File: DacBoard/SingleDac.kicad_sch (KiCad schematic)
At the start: 1 part, among them U5 AD5725

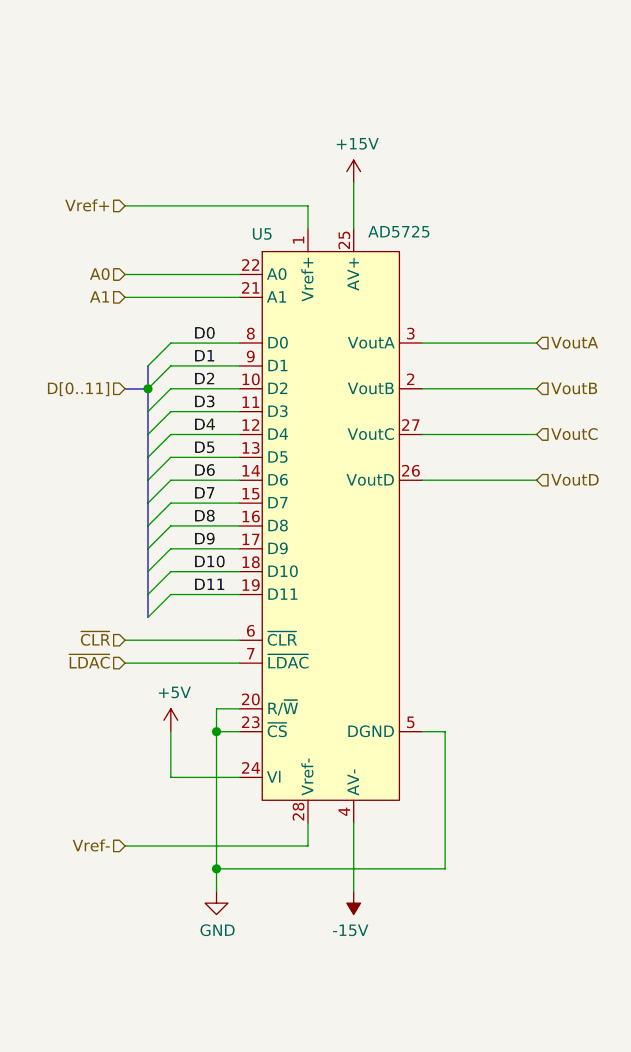
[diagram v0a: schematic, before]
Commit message: Changed data bus to single wires
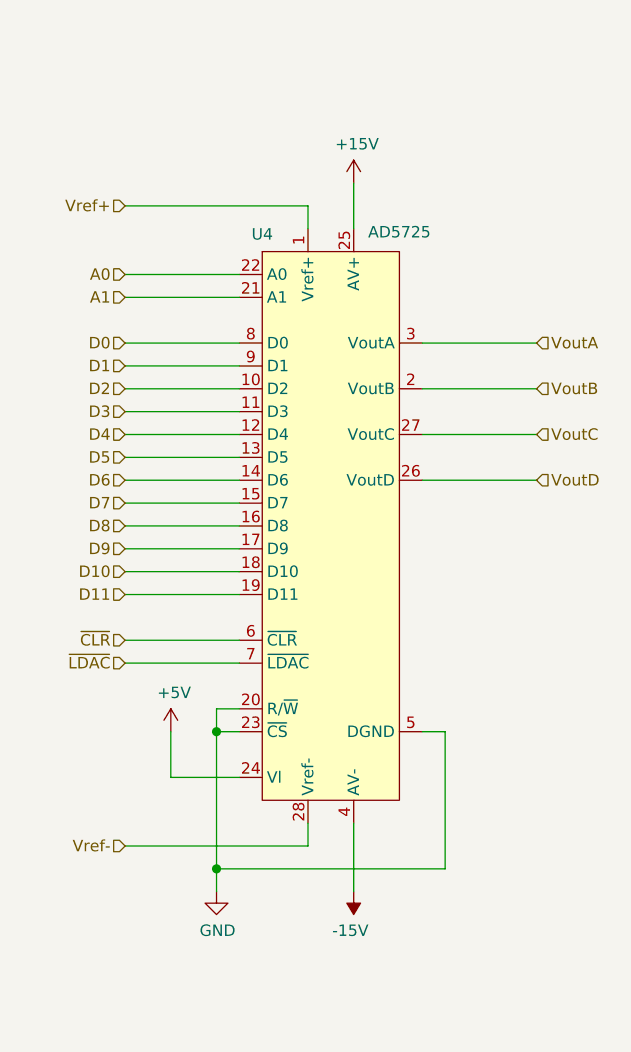
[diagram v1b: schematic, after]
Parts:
- renumbered U5 to U4

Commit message: Added bypass caps and moved PWR_FLAGs around
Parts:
- added C8, C9: 100n, symbol Device:C_Small
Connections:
- net +15V: now also C8.1, C8.2
- net -15V: now also C9.1, C9.2
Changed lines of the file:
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@@
   (paper "A4")
   (junction (at 167.64 104.14) (diameter 1.016) (color 0 0 0 0))
-  (junction (at 167.64 119.38) (diameter 1.016) (color 0 0 0 0))
+  (junction (at 182.88 33.02) (diameter 1.016) (color 0 0 0 0))
+  (junction (at 182.88 43.18) (diameter 1.016) (color 0 0 0 0))
+  (junction (at 182.88 121.92) (diameter 1.016) (color 0 0 0 0))
+  (junction (at 182.88 132.08) (diameter 1.016) (color 0 0 0 0))
   (wire (pts (xy 157.48 45.72) (xy 177.8 45.72))
     (stroke (width 0) (type solid) (color 0 0 0 0))
@@
     (stroke (width 0) (type solid) (color 0 0 0 0))
   )
-  (wire (pts (xy 167.64 104.14) (xy 167.64 119.38))
+  (wire (pts (xy 167.64 104.14) (xy 167.64 111.76))
     (stroke (width 0) (type solid) (color 0 0 0 0))
   )
@@
     (stroke (width 0) (type solid) (color 0 0 0 0))
   )
-  (wire (pts (xy 167.64 119.38) (xy 167.64 121.92))
-    (stroke (width 0) (type solid) (color 0 0 0 0))
-  )
-  (wire (pts (xy 167.64 119.38) (xy 193.04 119.38))
-    (stroke (width 0) (type solid) (color 0 0 0 0))
-  )
   (wire (pts (xy 170.18 101.6) (xy 167.64 101.6))
     (stroke (width 0) (type solid) (color 0 0 0 0))
@@
     (stroke (width 0) (type solid) (color 0 0 0 0))
   )
-  (wire (pts (xy 177.8 114.3) (xy 177.8 116.84))
-    (stroke (width 0) (type solid) (color 0 0 0 0))
-  )
-  (wire (pts (xy 177.8 116.84) (xy 157.48 116.84))
+  (wire (pts (xy 177.8 114.3) (xy 177.8 119.38))
+    (stroke (width 0) (type solid) (color 0 0 0 0))
+  )
+  (wire (pts (xy 177.8 119.38) (xy 157.48 119.38))
+    (stroke (width 0) (type solid) (color 0 0 0 0))
+  )
+  (wire (pts (xy 182.88 33.02) (xy 182.88 43.18))
+    (stroke (width 0) (type solid) (color 0 0 0 0))
+  )
+  (wire (pts (xy 182.88 33.02) (xy 187.96 33.02))
     (stroke (width 0) (type solid) (color 0 0 0 0))
   )
@@
     (stroke (width 0) (type solid) (color 0 0 0 0))
   )
+  (wire (pts (xy 182.88 43.18) (xy 187.96 43.18))
+    (stroke (width 0) (type solid) (color 0 0 0 0))
+  )
   (wire (pts (xy 182.88 114.3) (xy 182.88 121.92))
     (stroke (width 0) (type solid) (color 0 0 0 0))
   )
+  (wire (pts (xy 182.88 121.92) (xy 187.96 121.92))
+    (stroke (width 0) (type solid) (color 0 0 0 0))
+  )
+  (wire (pts (xy 182.88 132.08) (xy 182.88 121.92))
+    (stroke (width 0) (type solid) (color 0 0 0 0))
+  )
+  (wire (pts (xy 182.88 132.08) (xy 187.96 132.08))
+    (stroke (width 0) (type solid) (color 0 0 0 0))
+  )
+  (wire (pts (xy 187.96 33.02) (xy 187.96 35.56))
+    (stroke (width 0) (type solid) (color 0 0 0 0))
+  )
+  (wire (pts (xy 187.96 43.18) (xy 187.96 40.64))
+    (stroke (width 0) (type solid) (color 0 0 0 0))
+  )
+  (wire (pts (xy 187.96 121.92) (xy 187.96 124.46))
+    (stroke (width 0) (type solid) (color 0 0 0 0))
+  )
+  (wire (pts (xy 187.96 132.08) (xy 187.96 129.54))
+    (stroke (width 0) (type solid) (color 0 0 0 0))
+  )
   (wire (pts (xy 190.5 60.96) (xy 203.2 60.96))
     (stroke (width 0) (type solid) (color 0 0 0 0))
@@
     (stroke (width 0) (type solid) (color 0 0 0 0))
   )
-  (wire (pts (xy 193.04 104.14) (xy 193.04 119.38))
+  (wire (pts (xy 193.04 104.14) (xy 193.04 109.22))
     (stroke (width 0) (type solid) (color 0 0 0 0))
   )
@@
     (effects (font (size 1.27 1.27)) (justify right))
   )
-  (hierarchical_label "Vref-" (shape input) (at 157.48 116.84 180)
-    (effects (font (size 1.27 1.27)) (justify right))
-  )
-  (hierarchical_label "VoutA" (shape input) (at 203.2 60.96 0)
+  (hierarchical_label "Vref-" (shape input) (at 157.48 119.38 180)
+    (effects (font (size 1.27 1.27)) (justify right))
+  )
+  (hierarchical_label "VoutA" (shape output) (at 203.2 60.96 0)
     (effects (font (size 1.27 1.27)) (justify left))
   )
-  (hierarchical_label "VoutB" (shape input) (at 203.2 66.04 0)
+  (hierarchical_label "VoutB" (shape output) (at 203.2 66.04 0)
     (effects (font (size 1.27 1.27)) (justify left))
   )
-  (hierarchical_label "VoutC" (shape input) (at 203.2 71.12 0)
+  (hierarchical_label "VoutC" (shape output) (at 203.2 71.12 0)
     (effects (font (size 1.27 1.27)) (justify left))
   )
-  (hierarchical_label "VoutD" (shape input) (at 203.2 76.2 0)
+  (hierarchical_label "VoutD" (shape output) (at 203.2 76.2 0)
     (effects (font (size 1.27 1.27)) (justify left))
   )
@@
     (pin "1")
   )
-  (symbol (lib_id "power:+15V") (at 182.88 43.18 0)
-    (in_bom yes) (on_board yes)
-    (property "Reference" "#PWR05" (id 0) (at 182.88 46.99 0)
-      (effects (font (size 1.27 1.27)) hide)
-    )
-    (property "Value" "+15V" (id 1) (at 183.2483 38.8556 0))
-    (property "Footprint" "" (id 2) (at 182.88 43.18 0)
-      (effects (font (size 1.27 1.27)) hide)
-    )
-    (property "Datasheet" "" (id 3) (at 182.88 43.18 0)
-      (effects (font (size 1.27 1.27)) hide)
-    )
-    (pin "1")
-  )
-  (symbol (lib_id "power:-15V") (at 182.88 121.92 180)
-    (in_bom yes) (on_board yes)
-    (property "Reference" "#PWR06" (id 0) (at 182.88 124.46 0)
-      (effects (font (size 1.27 1.27)) hide)
-    )
-    (property "Value" "-15V" (id 1) (at 182.5117 126.2444 0))
-    (property "Footprint" "" (id 2) (at 182.88 121.92 0)
-      (effects (font (size 1.27 1.27)) hide)
-    )
-    (property "Datasheet" "" (id 3) (at 182.88 121.92 0)
-      (effects (font (size 1.27 1.27)) hide)
-    )
-    (pin "1")
-  )
-  (symbol (lib_id "power:GND") (at 167.64 121.92 0)
-    (in_bom yes) (on_board yes)
-    (property "Reference" "#PWR04" (id 0) (at 167.64 128.27 0)
-      (effects (font (size 1.27 1.27)) hide)
-    )
-    (property "Value" "GND" (id 1) (at 167.7543 126.2444 0))
-    (property "Footprint" "" (id 2) (at 167.64 121.92 0)
-      (effects (font (size 1.27 1.27)) hide)
-    )
-    (property "Datasheet" "" (id 3) (at 167.64 121.92 0)
-      (effects (font (size 1.27 1.27)) hide)
-    )
-    (pin "1")
+  (symbol (lib_id "power:+15V") (at 182.88 33.02 0)
+    (in_bom yes) (on_board yes)
+    (property "Reference" "#PWR05" (id 0) (at 182.88 36.83 0)
+      (effects (font (size 1.27 1.27)) hide)
+    )
+    (property "Value" "+15V" (id 1) (at 183.2483 28.6956 0))
+    (property "Footprint" "" (id 2) (at 182.88 33.02 0)
+      (effects (font (size 1.27 1.27)) hide)
+    )
+    (property "Datasheet" "" (id 3) (at 182.88 33.02 0)
+      (effects (font (size 1.27 1.27)) hide)
+    )
+    (pin "1")
+  )
+  (symbol (lib_id "power:-15V") (at 182.88 132.08 180)
+    (in_bom yes) (on_board yes)
+    (property "Reference" "#PWR06" (id 0) (at 182.88 134.62 0)
+      (effects (font (size 1.27 1.27)) hide)
+    )
+    (property "Value" "-15V" (id 1) (at 182.5117 136.4044 0))
+    (property "Footprint" "" (id 2) (at 182.88 132.08 0)
+      (effects (font (size 1.27 1.27)) hide)
+    )
+    (property "Datasheet" "" (id 3) (at 182.88 132.08 0)
+      (effects (font (size 1.27 1.27)) hide)
+    )
+    (pin "1")
+  )
+  (symbol (lib_id "power:GND") (at 167.64 111.76 0)
+    (in_bom yes) (on_board yes)
+    (property "Reference" "#PWR04" (id 0) (at 167.64 118.11 0)
+      (effects (font (size 1.27 1.27)) hide)
+    )
+    (property "Value" "GND" (id 1) (at 167.7543 116.0844 0))
+    (property "Footprint" "" (id 2) (at 167.64 111.76 0)
+      (effects (font (size 1.27 1.27)) hide)
+    )
+    (property "Datasheet" "" (id 3) (at 167.64 111.76 0)
+      (effects (font (size 1.27 1.27)) hide)
+    )
+    (pin "1")
+  )
+  (symbol (lib_id "power:GND") (at 193.04 109.22 0)
+    (in_bom yes) (on_board yes)
+    (property "Reference" "#PWR07" (id 0) (at 193.04 115.57 0)
+      (effects (font (size 1.27 1.27)) hide)
+    )
+    (property "Value" "GND" (id 1) (at 193.1543 113.5444 0))
+    (property "Footprint" "" (id 2) (at 193.04 109.22 0)
+      (effects (font (size 1.27 1.27)) hide)
+    )
+    (property "Datasheet" "" (id 3) (at 193.04 109.22 0)
+      (effects (font (size 1.27 1.27)) hide)
+    )
+    (pin "1")
+  )
+  (symbol (lib_id "Device:C_Small") (at 187.96 38.1 0)
+    (in_bom yes) (on_board yes)
+    (property "Reference" "C8" (id 0) (at 190.2842 36.9506 0)
+      (effects (font (size 1.27 1.27)) (justify left))
+    )
+    (property "Value" "100n" (id 1) (at 190.2968 39.243 0)
+      (effects (font (size 1.27 1.27)) (justify left))
+    )
+    (property "Footprint" "" (id 2) (at 187.96 38.1 0)
+      (effects (font (size 1.27 1.27)) hide)
+    )
+    (property "Datasheet" "~" (id 3) (at 187.96 38.1 0)
+      (effects (font (size 1.27 1.27)) hide)
+    )
+    (pin "1")
+    (pin "2")
+  )
+  (symbol (lib_id "Device:C_Small") (at 187.96 127 0)
+    (in_bom yes) (on_board yes)
+    (property "Reference" "C9" (id 0) (at 190.2842 125.8506 0)
+      (effects (font (size 1.27 1.27)) (justify left))
+    )
+    (property "Value" "100n" (id 1) (at 190.2968 128.143 0)
+      (effects (font (size 1.27 1.27)) (justify left))
+    )
+    (property "Footprint" "" (id 2) (at 187.96 127 0)
+      (effects (font (size 1.27 1.27)) hide)
+    )
+    (property "Datasheet" "~" (id 3) (at 187.96 127 0)
+      (effects (font (size 1.27 1.27)) hide)
+    )
+    (pin "1")
+    (pin "2")
   )
   (symbol (lib_id "Unichip:AD5725") (at 180.34 50.8 0)

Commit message: Fixed description of enable signal generators
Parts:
- renumbered C8 to C10, C9 to C11, U4 to U5
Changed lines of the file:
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@@
   (symbol (lib_id "power:+5V") (at 162.56 104.14 0)
     (in_bom yes) (on_board yes)
-    (property "Reference" "#PWR03" (id 0) (at 162.56 107.95 0)
+    (property "Reference" "#PWR0129" (id 0) (at 162.56 107.95 0)
       (effects (font (size 1.27 1.27)) hide)
     )
@@
   (symbol (lib_id "power:+15V") (at 182.88 33.02 0)
     (in_bom yes) (on_board yes)
-    (property "Reference" "#PWR05" (id 0) (at 182.88 36.83 0)
+    (property "Reference" "#PWR0128" (id 0) (at 182.88 36.83 0)
       (effects (font (size 1.27 1.27)) hide)
     )
@@
   (symbol (lib_id "power:-15V") (at 182.88 132.08 180)
     (in_bom yes) (on_board yes)
-    (property "Reference" "#PWR06" (id 0) (at 182.88 134.62 0)
+    (property "Reference" "#PWR0131" (id 0) (at 182.88 134.62 0)
       (effects (font (size 1.27 1.27)) hide)
     )
@@
   (symbol (lib_id "power:GND") (at 167.64 111.76 0)
     (in_bom yes) (on_board yes)
-    (property "Reference" "#PWR04" (id 0) (at 167.64 118.11 0)
+    (property "Reference" "#PWR0130" (id 0) (at 167.64 118.11 0)
       (effects (font (size 1.27 1.27)) hide)
     )
@@
   (symbol (lib_id "power:GND") (at 193.04 109.22 0)
     (in_bom yes) (on_board yes)
-    (property "Reference" "#PWR07" (id 0) (at 193.04 115.57 0)
+    (property "Reference" "#PWR08" (id 0) (at 193.04 115.57 0)
       (effects (font (size 1.27 1.27)) hide)
     )
@@
   (symbol (lib_id "Device:C_Small") (at 187.96 38.1 0)
     (in_bom yes) (on_board yes)
-    (property "Reference" "C8" (id 0) (at 190.2842 36.9506 0)
+    (property "Reference" "C10" (id 0) (at 190.2842 36.9506 0)
       (effects (font (size 1.27 1.27)) (justify left))
     )
@@
   (symbol (lib_id "Device:C_Small") (at 187.96 127 0)
     (in_bom yes) (on_board yes)
-    (property "Reference" "C9" (id 0) (at 190.2842 125.8506 0)
+    (property "Reference" "C11" (id 0) (at 190.2842 125.8506 0)
       (effects (font (size 1.27 1.27)) (justify left))
     )
@@
   (symbol (lib_id "Unichip:AD5725") (at 180.34 50.8 0)
     (in_bom yes) (on_board yes)
-    (property "Reference" "U4" (id 0) (at 172.72 48.8758 0))
+    (property "Reference" "U5" (id 0) (at 172.72 48.8758 0))
     (property "Value" "AD5725" (id 1) (at 187.96 48.6345 0))
     (property "Footprint" "Package_SO:SSOP-28_5.3x10.2mm_P0.65mm" (id 2) (at 170.18 77.47 0)
